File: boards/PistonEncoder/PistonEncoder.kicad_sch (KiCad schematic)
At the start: 32 parts, among them J1 ISP, J2 Ext, J3 PWR, J4 LED1, J5 LED2, J6 Pistons1, J7 Pistons2, J8 BoardCon, Q1 BC547, U1 ATmega48-20P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

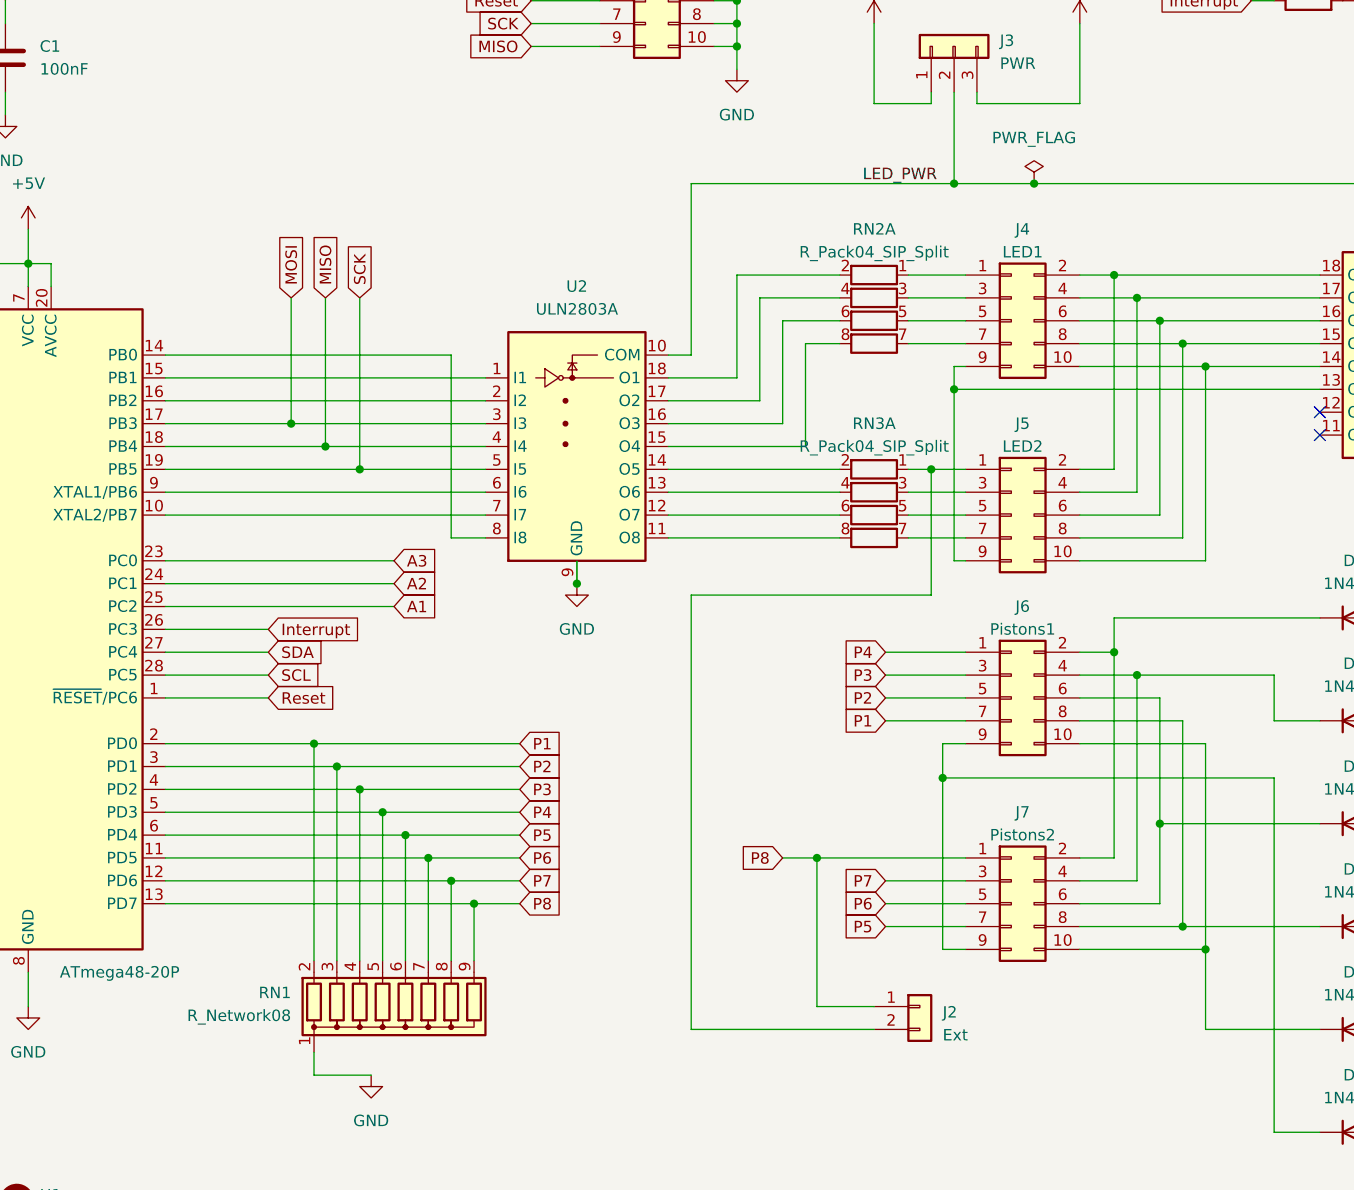
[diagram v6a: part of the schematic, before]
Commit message: Added bypass caps to power supplies, use cheaper MAX232 IC.
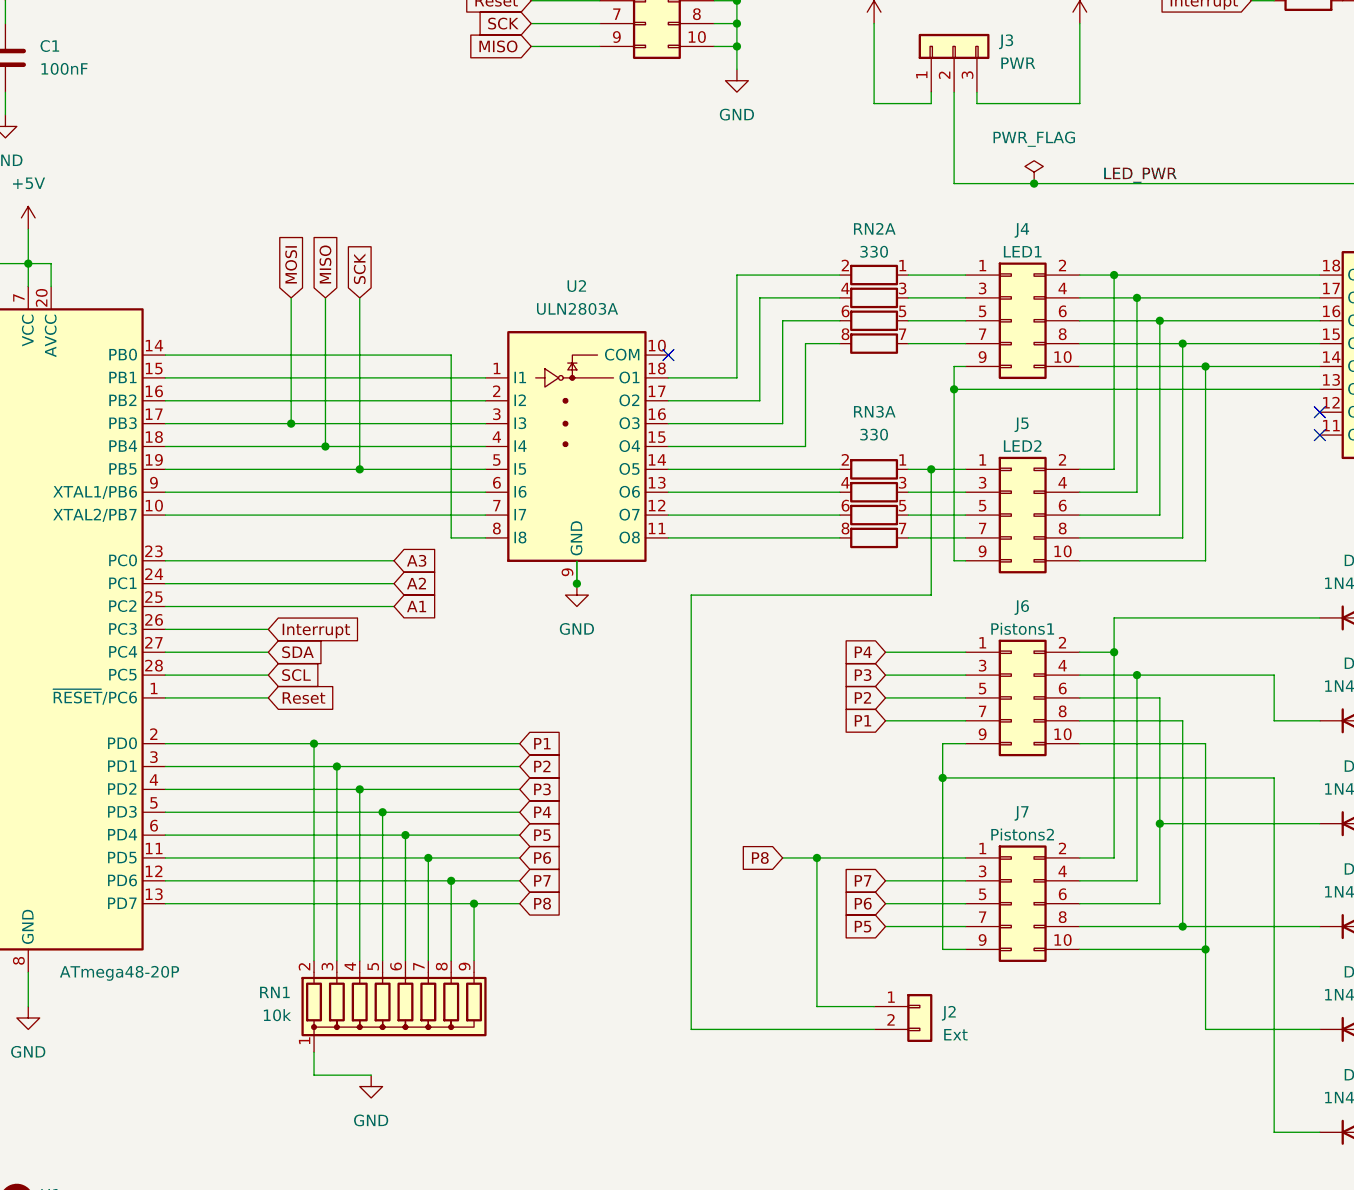
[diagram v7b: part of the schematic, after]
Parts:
- RN1: value R_Network08 -> 10k
- RN2, RN3: value R_Pack04_SIP_Split -> 330
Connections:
- net LED_PWR: no longer U2.10 (COM)
- no-connect marks 7 -> 8
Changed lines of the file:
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@@
 	)
 	(junction
-		(at 142.24 54.61)
-		(diameter 0)
-		(color 0 0 0 0)
-	)
-	(junction
 		(at 195.58 102.87)
 		(diameter 0)
@@
 	)
 	(no_connect
+		(at 110.49 73.66)
+	)
+	(no_connect
 		(at 208.28 35.56)
 	)
@@
 	(wire
 		(pts
-			(xy 142.24 54.61) (xy 113.03 54.61)
-		)
-		(stroke
-			(width 0)
-			(type default)
-		)
-	)
-	(wire
-		(pts
 			(xy 214.63 26.67) (xy 223.52 26.67)
 		)
@@
 	(wire
 		(pts
-			(xy 113.03 54.61) (xy 113.03 73.66)
-		)
-		(stroke
-			(width 0)
-			(type default)
-		)
-	)
-	(wire
-		(pts
 			(xy 78.74 124.46) (xy 93.98 124.46)
 		)
@@
 	(wire
 		(pts
-			(xy 110.49 73.66) (xy 113.03 73.66)
-		)
-		(stroke
-			(width 0)
-			(type default)
-		)
-	)
-	(wire
-		(pts
 			(xy 267.97 106.68) (xy 267.97 104.14)
 		)
@@
 	)
 	(label "LED_PWR"
-		(at 132.08 54.61 0)
+		(at 158.75 54.61 0)
 		(fields_autoplaced yes)
 		(effects
@@
 			)
 		)
-		(property "Value" "R_Pack04_SIP_Split"
+		(property "Value" "330"
 			(at 133.35 88.9 90)
 			(effects
@@
 			)
 		)
-		(property "Value" "R_Pack04_SIP_Split"
+		(property "Value" "330"
 			(at 133.35 69.85 90)
 			(effects
@@
 			)
 		)
-		(property "Value" "R_Pack04_SIP_Split"
+		(property "Value" "330"
 			(at 133.35 64.77 90)
 			(effects
@@
 			)
 		)
-		(property "Value" "R_Network08"
+		(property "Value" "10k"
 			(at 68.58 147.0659 0)
 			(effects
@@
 			)
 		)
-		(property "Value" "R_Pack04_SIP_Split"
+		(property "Value" "330"
 			(at 133.35 67.31 90)
 			(effects
@@
 			)
 		)
-		(property "Value" "R_Pack04_SIP_Split"
+		(property "Value" "330"
 			(at 133.35 62.23 90)
 			(effects
@@
 		(fields_autoplaced yes)
 		(property "Reference" "RN3"
-			(at 133.35 81.28 90)
+			(at 133.35 80.01 90)
 			(effects
 				(font
@@
 			)
 		)
-		(property "Value" "R_Pack04_SIP_Split"
-			(at 133.35 83.82 90)
+		(property "Value" "330"
+			(at 133.35 82.55 90)
 			(effects
 				(font
@@
 			)
 		)
-		(property "Value" "R_Pack04_SIP_Split"
+		(property "Value" "330"
 			(at 133.35 91.44 90)
 			(effects
@@
 			)
 		)
-		(property "Value" "R_Pack04_SIP_Split"
+		(property "Value" "330"
 			(at 133.35 86.36 90)
 			(effects

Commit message: Updated design rules to 0.32mm template and exported Gerber files
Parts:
- C2: footprint Capacitor_THT:C_Radial_D6.3mm_H7.0mm_P2.50mm -> Capacitor_THT:C_Radial_D5.0mm_H11.0mm_P2.00mm
- R1: footprint Resistor_THT:R_Axial_DIN0204_L3.6mm_D1.6mm_P7.62mm_Horizontal -> Resistor_THT:R_Axial_DIN0207_L6.3mm_D2.5mm_P10.16mm_Horizontal
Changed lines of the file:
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@@
 			)
 		)
-		(property "Footprint" "Capacitor_THT:C_Radial_D6.3mm_H7.0mm_P2.50mm"
+		(property "Footprint" "Capacitor_THT:C_Radial_D5.0mm_H11.0mm_P2.00mm"
 			(at 251.1552 43.18 0)
 			(effects
@@
 			)
 		)
-		(property "Footprint" "Resistor_THT:R_Axial_DIN0204_L3.6mm_D1.6mm_P7.62mm_Horizontal"
+		(property "Footprint" "Resistor_THT:R_Axial_DIN0207_L6.3mm_D2.5mm_P10.16mm_Horizontal"
 			(at 181.61 36.068 90)
 			(effects
